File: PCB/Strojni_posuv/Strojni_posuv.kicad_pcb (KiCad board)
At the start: 2 copper layers, 227 x 80 mm, 140 parts, among them IC1 TB6600HG, J1 Conn_01x20_Pin, J10 Conn_01x05_Socket, J11 Volne_IO_Power, J12 Button_conf, J2 Button_power_A, J3 OUT1, J4 OUT2, J5 POWER, J6 Button_power_B, J7 Button_maxL, J8 Volne_IO, J9 Button_maxR, Q1 BSS138, Q2 BSS138, Q3 BSS138, Q4 BSS138, Q5 BSS138, Q6 BSS138, Q7 BC847, Q8 BSS138, Q9 BSS138, SW1 SW_SPDT_MSM, SW4 SW_SPDT, SW5 RotaryEncoder_Switch, SW6 Emergency_stop, U1 STM32F103RBTx, U7 74HC14, U8 TPS62822DLC, Y1 16MHz

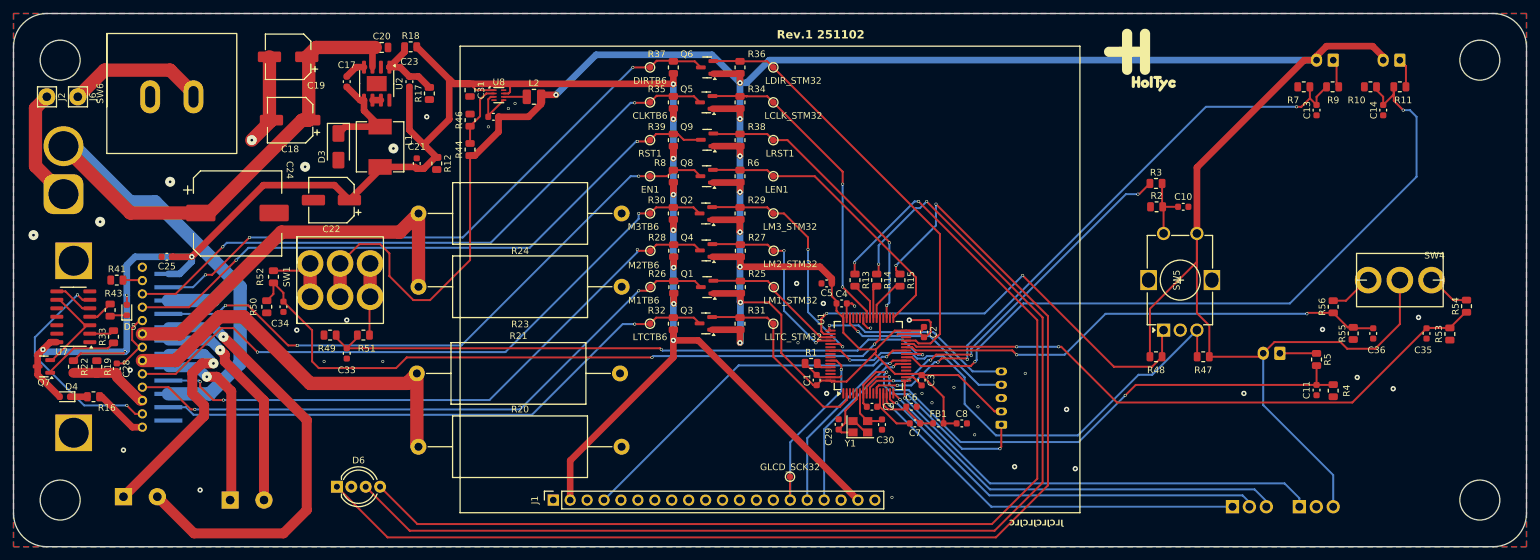
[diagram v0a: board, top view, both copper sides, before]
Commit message: Small changes
I needed to update the board to version 9.0 and relocate some silkscreen items
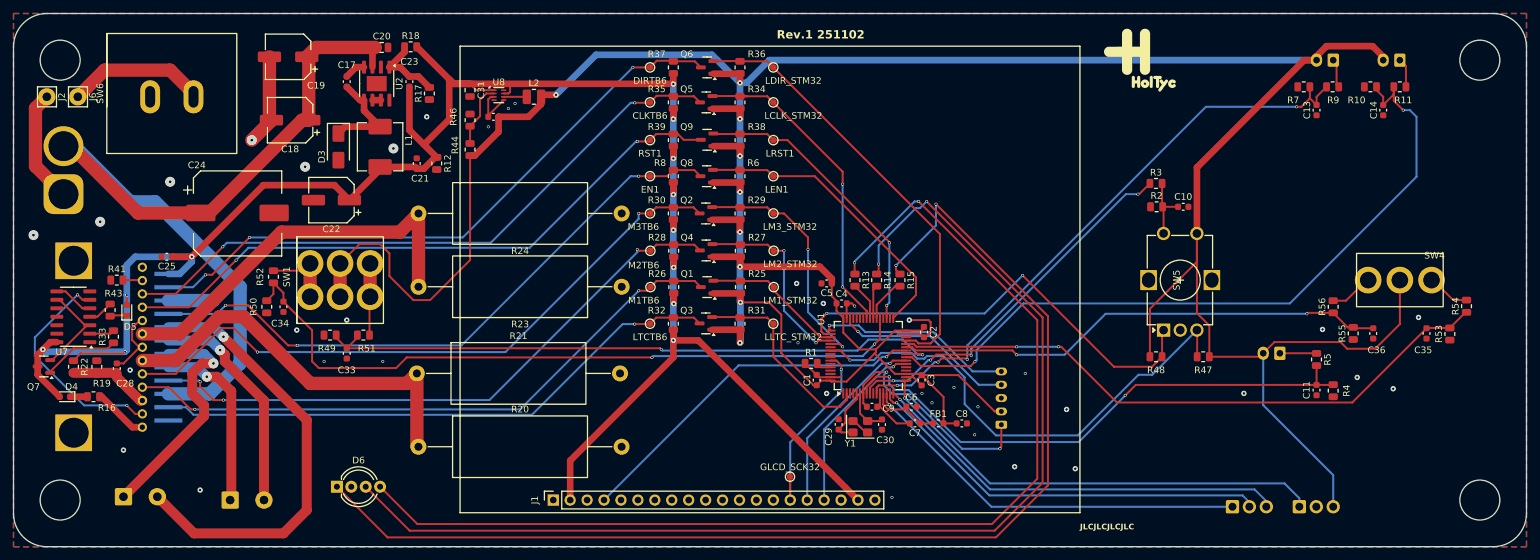
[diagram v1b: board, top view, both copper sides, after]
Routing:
- net unconnected-(U1-PA9-Pad42): track 2.26 -> 0.00 mm, vias 1 -> 0

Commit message: Numpad + small changes
I added numpad and add some description to components
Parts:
- added Numpad1: Conn_01x08_Socket, Connector_PinSocket_2.54mm:PinSocket_1x08_P2.54mm_Vertical, F.Cu at (165.7, 45.0)
- Programming conn: renamed from J10; moved to F.Cu
- moved G*** 6.42 mm to (204.5, 43.5)
- moved C4 1.75 mm to (158.5, 73.5)
- moved C2 1.73 mm to (172.7, 76.1)
- moved C5 1.50 mm to (156.5, 70.5)
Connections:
- U1 pad 30: unconnected-(U1-PB11-Pad30) -> NumPB11
- U1 pad 34: unconnected-(U1-PB13-Pad34) -> NumPB13
- U1 pad 36: unconnected-(U1-PB15-Pad36) -> NumPB15
- U1 pad 42: unconnected-(U1-PA9-Pad42) -> NumPA9
- U1 pad 43: unconnected-(U1-PA10-Pad43) -> NumPA10
- U1 pad 44: unconnected-(U1-PA11-Pad44) -> NumPA11
- U1 pad 45: unconnected-(U1-PA12-Pad45) -> NumPA12
- U1 pad 54: unconnected-(U1-PD2-Pad54) -> NumPD2
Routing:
- net NumPB11: track 0.00 -> 45.6 mm, vias 0 -> 1
- net NumPD2: track 0.00 -> 44.3 mm, vias 0 -> 1
- net NumPA9: track 0.00 -> 43.0 mm, vias 0 -> 1
- net NumPB13: track 0.00 -> 40.9 mm, vias 0 -> 1
- net NumPB15: track 0.00 -> 40.8 mm, vias 0 -> 1
- net NumPA10: track 0.00 -> 37.1 mm, vias 0 -> 1
- net NumPA11: track 0.00 -> 36.3 mm, vias 0 -> 1
- net NumPA12: track 0.00 -> 35.5 mm, vias 0 -> 1
- net Reset: track 44.7 -> 48.6 mm
- net STEP_STM: track 48.6 -> 51.8 mm
- net GND: track 66.3 -> 69.4 mm, vias 38 -> 47
- net Enable: track 44.6 -> 46.4 mm
- net Net-(D6-RK): track 167.9 -> 166.7 mm
- net M1_STM: track 21.4 -> 22.2 mm
- net Net-(D6-GK): track 171.0 -> 170.3 mm
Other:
- board text added: "+"
- board text added: "3V3"
- board text added: "Developed by: Jan Holy"
- board text added: "Doraz LEVA strana"
- board text added: "Doraz PRAVA strana"
- board text added: "GND"
- board text added: "NRST"
- board text added: "Numpad"
- board text added: "PA0"
- board text added: "PA1"
- board text added: "PA2"
- board text added: "PA3"
- board text added: "Rev.1 251608"
- board text added: "SWCLK"
- board text added: "SWDIO"
- board text added: "Tlacitko"
- board text added: "o o o"
- board text added: "o o o o o"
- board text removed: "Rev.1 251102"
